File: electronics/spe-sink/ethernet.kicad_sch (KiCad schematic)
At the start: 36 parts, among them U4 ADIN1110, X1 RH100-25.000-13-F-0715

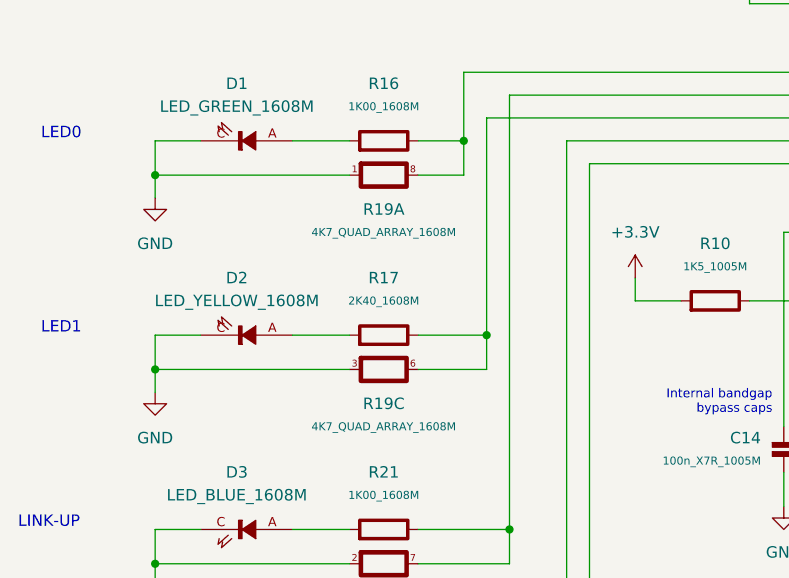
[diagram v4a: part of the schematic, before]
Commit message: PD sink PCB design 'finished', page cleanup, etc
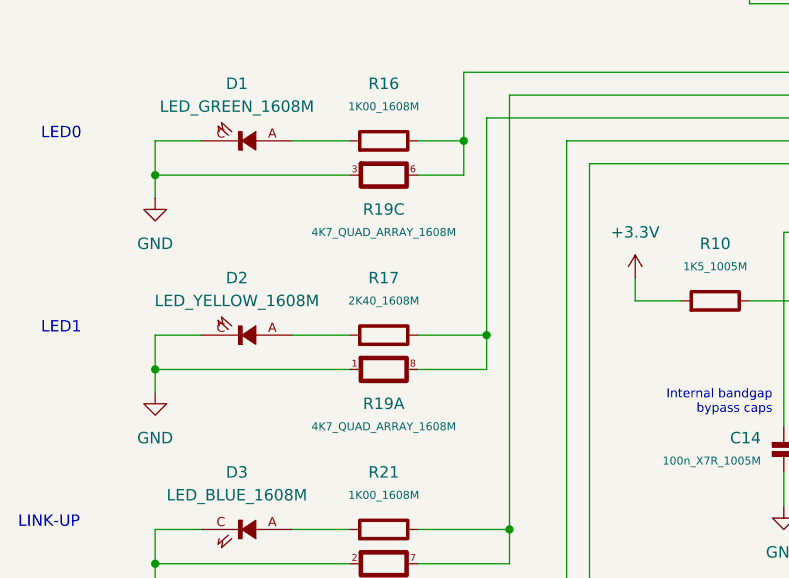
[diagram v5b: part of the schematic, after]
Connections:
- net GND: now also R19.1, R19.3; no longer R19.1, R19.3
- net at R16.2, U4.3 (LED_0): now also R19.6; no longer R19.8
- net at R17.2, U4.6 (LED_1): now also R19.8; no longer R19.6
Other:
- title: (none) -> ADIN1110 SPE Transciever
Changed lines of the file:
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@@
 (kicad_sch (version 20230121) (generator eeschema)
   (paper "A4")
+  (title_block
+    (title "ADIN1110 SPE Transciever")
+    (date "2023-08-16")
+    (rev "V1.0")
+    (comment 1 "All configuration pins are left in default state")
+    (comment 2 "Aims to maintain compatibility with Sparkfun ADIN1110 board")
+  )
   (junction (at 223.52 24.13) (diameter 0) (color 0 0 0 0)
   )
@@
     )
   )
-  (symbol (lib_id "appli_resistor:4K7_QUAD_ARRAY_1608M") (at 53.34 82.55 90) (unit 1)
+  (symbol (lib_id "appli_resistor:4K7_QUAD_ARRAY_1608M") (at 53.34 82.55 90) (unit 3)
     (in_bom yes) (on_board yes) (dnp no)
     (property "Reference" "R19" (at 57.15 86.36 90)
@@
       (project "spe-sink"
         (path "/f0a501c7-1ad1-4c59-9255-3d6aa4545d8b/c444fd40-2442-4c73-bf48-a4aa084e5cc8"
-          (reference "R19") (unit 1)
+          (reference "R19") (unit 3)
         )
       )
@@
     )
   )
-  (symbol (lib_id "appli_resistor:4K7_QUAD_ARRAY_1608M") (at 53.34 104.14 90) (unit 3)
+  (symbol (lib_id "appli_resistor:4K7_QUAD_ARRAY_1608M") (at 53.34 104.14 90) (unit 1)
     (in_bom yes) (on_board yes) (dnp no)
     (property "Reference" "R19" (at 57.15 107.95 90)
@@
       (project "spe-sink"
         (path "/f0a501c7-1ad1-4c59-9255-3d6aa4545d8b/c444fd40-2442-4c73-bf48-a4aa084e5cc8"
-          (reference "R19") (unit 3)
+          (reference "R19") (unit 1)
         )
       )
